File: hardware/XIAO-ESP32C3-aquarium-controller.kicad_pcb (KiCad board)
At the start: 2 copper layers, 72 x 99 mm, 43 parts, among them J1 Conn_01x02, J2 Conn_01x07, J3 Conn_01x06, J4 Conn_01x03, J5 Conn_01x03, K1 SANYOU_SRD_Form_C, K2 SANYOU_SRD_Form_C, K3 SANYOU_SRD_Form_C, Q1 AO3400A, Q2 AO3400A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

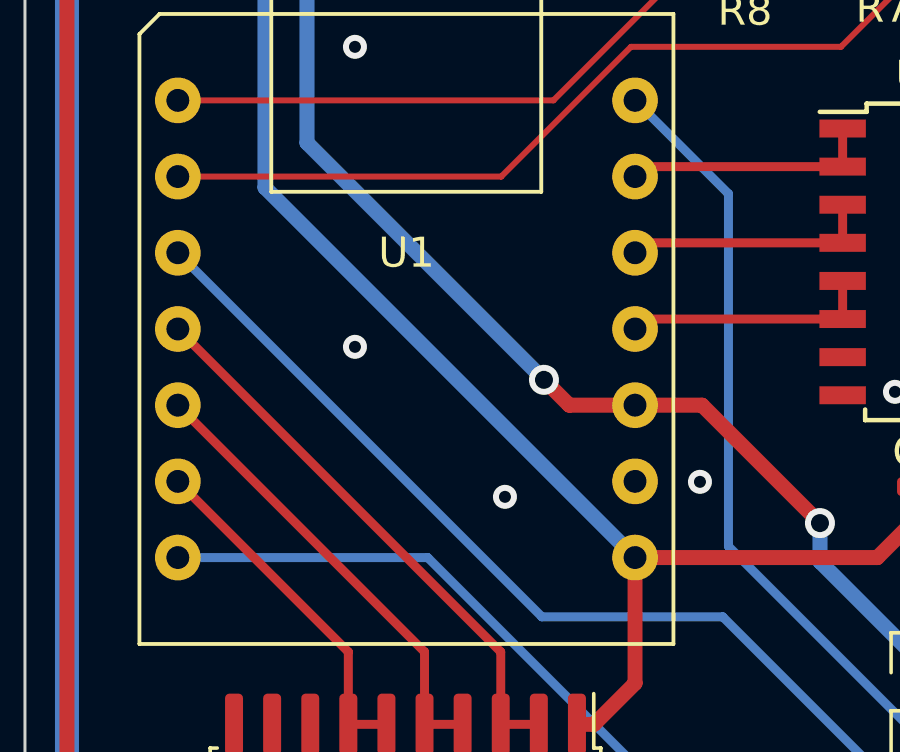
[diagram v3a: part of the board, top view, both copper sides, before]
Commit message: capacitor for ESP32C3
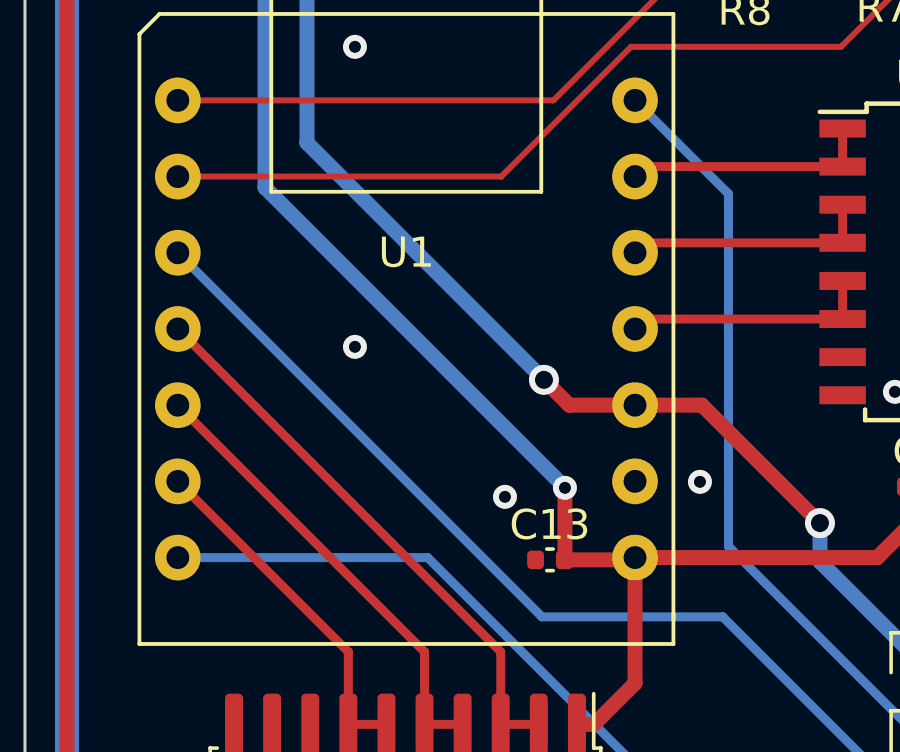
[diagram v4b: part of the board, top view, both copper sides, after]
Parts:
- added C13: 4.7uF, Capacitor_SMD:C_0402_1005Metric, F.Cu at (48.1, 84.1)
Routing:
- net +5V: track 502.7 -> 504.2 mm, vias 6 -> 7
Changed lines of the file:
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@@
+    )
+  )
+  (footprint "Capacitor_SMD:C_0402_1005Metric" (layer "F.Cu")
+    (at 48.1 84.1)
+    (descr "Capacitor SMD 0402 (1005 Metric), square (rectangular) end terminal, IPC_7351 nominal, (Body size source: IPC-SM-782 page 76, https://www.pcb-3d.com/wordpress/wp-content/uploads/ipc-sm-782a_amendment_1_and_2.pdf), generated with kicad-footprint-generator")
+    (tags "capacitor")
+    (property "JLCPCB Part #" "C23733")
+    (property "Sheetfile" "XIAO-ESP32C3-aquarium-controller.kicad_sch")
+    (property "Sheetname" "")
+    (property "ki_description" "Unpolarized capacitor")
+    (property "ki_keywords" "cap capacitor")
+    (attr smd)
+    (fp_text reference "C13" (at 0 -1.16) (layer "F.SilkS")
+        (effects (font (size 1 1) (thickness 0.15)))
+    )
+    (fp_text value "4.7uF" (at 0 1.16) (layer "F.Fab")
+        (effects (font (size 1 1) (thickness 0.15)))
+    )
+    (fp_text user "${REFERENCE}" (at 0 0) (layer "F.Fab")
+        (effects (font (size 0.25 0.25) (thickness 0.04)))
+    )
+    (fp_line (start -0.107836 -0.36) (end 0.107836 -0.36)
+      (stroke (width 0.12) (type solid)) (layer "F.SilkS"))
+    (fp_line (start -0.107836 0.36) (end 0.107836 0.36)
+      (stroke (width 0.12) (type solid)) (layer "F.SilkS"))
+    (fp_line (start -0.91 -0.46) (end 0.91 -0.46)
+      (stroke (width 0.05) (type solid)) (layer "F.CrtYd"))
+    (fp_line (start -0.91 0.46) (end -0.91 -0.46)
+      (stroke (width 0.05) (type solid)) (layer "F.CrtYd"))
+    (fp_line (start 0.91 -0.46) (end 0.91 0.46)
+      (stroke (width 0.05) (type solid)) (layer "F.CrtYd"))
+    (fp_line (start 0.91 0.46) (end -0.91 0.46)
+      (stroke (width 0.05) (type solid)) (layer "F.CrtYd"))
+    (fp_line (start -0.5 -0.25) (end 0.5 -0.25)
+      (stroke (width 0.1) (type solid)) (layer "F.Fab"))
+    (fp_line (start -0.5 0.25) (end -0.5 -0.25)
+      (stroke (width 0.1) (type solid)) (layer "F.Fab"))
+    (fp_line (start 0.5 -0.25) (end 0.5 0.25)
+      (stroke (width 0.1) (type solid)) (layer "F.Fab"))
+    (fp_line (start 0.5 0.25) (end -0.5 0.25)
+      (stroke (width 0.1) (type solid)) (layer "F.Fab"))
+    (pad "1" smd roundrect (at -0.48 0) (size 0.56 0.62) (layers "F.Cu" "F.Paste" "F.Mask") (roundrect_rratio 0.25)
+      (net 2 "GND") (pintype "passive"))
+    (pad "2" smd roundrect (at 0.48 0) (size 0.56 0.62) (layers "F.Cu" "F.Paste" "F.Mask") (roundrect_rratio 0.25)
+      (net 1 "+5V") (pintype "passive"))
+    (model "${KICAD6_3DMODEL_DIR}/Capacitor_SMD.3dshapes/C_0402_1005Metric.wrl"
+      (offset (xyz 0 0 0))
+      (scale (xyz 1 1 1))
+      (rotate (xyz 0 0 0))
     )
   )
@@
   (segment (start 68.062 68.25) (end 67.975 68.163) (width 0.5) (layer "F.Cu") (net 1))
   (segment locked (start 48.11 122.51) (end 49.9 124.3) (width 0.5) (layer "F.Cu") (net 1))
+  (segment (start 48.58 84.1) (end 50.86025 84.1) (width 0.5) (layer "F.Cu") (net 1))
   (segment (start 42.9035 35.1965) (end 34.481621 43.618379) (width 1.5) (layer "F.Cu") (net 1))
   (segment (start 68.43 121.717) (end 68.43 115.653) (width 0.8) (layer "F.Cu") (net 1))
@@
   (segment (start 66.277 113.5) (end 66.277 109.855) (width 0.5) (layer "F.Cu") (net 1))
   (segment (start 34 57.6) (end 33.6 57.6) (width 0.5) (layer "F.Cu") (net 1))
+  (segment (start 48.6 84.08) (end 48.58 84.1) (width 0.5) (layer "F.Cu") (net 1))
   (segment (start 68.3 100.634) (end 67.858 100.634) (width 0.5) (layer "F.Cu") (net 1))
   (segment (start 32 119.8) (end 36.4 124.2) (width 0.5) (layer "F.Cu") (net 1))
@@
   (segment locked (start 58.27 121.717) (end 61.153 124.6) (width 0.8) (layer "F.Cu") (net 1))
   (segment (start 48.999 89.584) (end 48.999 98.884) (width 0.5) (layer "F.Cu") (net 1))
+  (segment (start 50.86025 84.1) (end 50.93575 84.0245) (width 0.5) (layer "F.Cu") (net 1))
+  (segment (start 48.6 81.7) (end 48.6 84.08) (width 0.5) (layer "F.Cu") (net 1))
   (segment (start 67.858 100.634) (end 67.808 100.584) (width 0.5) (layer "F.Cu") (net 1))
   (segment (start 48.11 114.915) (end 46.695 113.5) (width 0.5) (layer "F.Cu") (net 1))
@@
   (segment (start 73.637 100.634) (end 68.3 100.634) (width 0.5) (layer "F.Cu") (net 1))
   (via (at 68 113.3) (size 0.8) (drill 0.4) (layers "F.Cu" "B.Cu") (net 1))
+  (via (at 48.6 81.7) (size 0.8) (drill 0.4) (layers "F.Cu" "B.Cu") (net 1))
   (via (at 34 57.6) (size 1) (drill 0.6) (layers "F.Cu" "B.Cu") (net 1))
   (via (at 68.3 98.3) (size 0.8) (drill 0.4) (layers "F.Cu" "B.Cu") (net 1))
@@
   (segment (start 68.25 63.55) (end 68 63.3) (width 0.8) (layer "B.Cu") (net 1))
   (segment (start 34.013 53.086) (end 34 53.099) (width 1.5) (layer "B.Cu") (net 1))
-  (segment (start 38.6 62.2) (end 38.6 71.68875) (width 0.5) (layer "B.Cu") (net 1))
   (segment (start 68.3 82.2) (end 68.25 82.15) (width 0.8) (layer "B.Cu") (net 1))
   (segment (start 33.6 57.6) (end 32 59.2) (width 0.8) (layer "B.Cu") (net 1))
@@
   (segment (start 48.11 122.51) (end 49.9 124.3) (width 0.8) (layer "B.Cu") (net 1))
   (segment (start 58.2685 121.717) (end 61.1515 124.6) (width 0.5) (layer "B.Cu") (net 1))
+  (segment (start 38.6 71.68875) (end 48.6 81.68875) (width 0.5) (layer "B.Cu") (net 1))
   (segment (start 68 113.3) (end 68.25 113.05) (width 0.8) (layer "B.Cu") (net 1))
   (segment (start 68.3 98.3) (end 68.25 98.25) (width 0.8) (layer "B.Cu") (net 1))
   (segment (start 34 57.6) (end 38.6 62.2) (width 0.5) (layer "B.Cu") (net 1))
   (segment (start 61.1515 124.6) (end 66.1985 124.6) (width 0.5) (layer "B.Cu") (net 1))
-  (segment (start 38.6 71.68875) (end 50.93575 84.0245) (width 0.5) (layer "B.Cu") (net 1))
   (segment (start 68.4285 122.37) (end 68.4285 121.717) (width 0.5) (layer "B.Cu") (net 1))
   (segment (start 48.11 121.717) (end 48.11 122.51) (width 0.8) (layer "B.Cu") (net 1))
@@
   (segment (start 68.25 82.15) (end 68.25 63.55) (width 0.8) (layer "B.Cu") (net 1))
   (segment (start 48.11 122.69) (end 48.11 121.717) (width 0.8) (layer "B.Cu") (net 1))
+  (segment (start 48.6 81.68875) (end 48.6 81.7) (width 0.5) (layer "B.Cu") (net 1))
+  (segment (start 38.6 62.2) (end 38.6 71.68875) (width 0.5) (layer "B.Cu") (net 1))
   (segment (start 68.25 98.35) (end 68.3 98.3) (width 0.8) (layer "B.Cu") (net 1))
   (segment (start 36.4 124.2) (end 46.6 124.2) (width 0.8) (layer "B.Cu") (net 1))
